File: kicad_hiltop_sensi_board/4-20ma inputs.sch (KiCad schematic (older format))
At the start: 44 parts, among them U12 MAX4194, U16 MAX4194, U19 MAX4194, U20 MAX4194

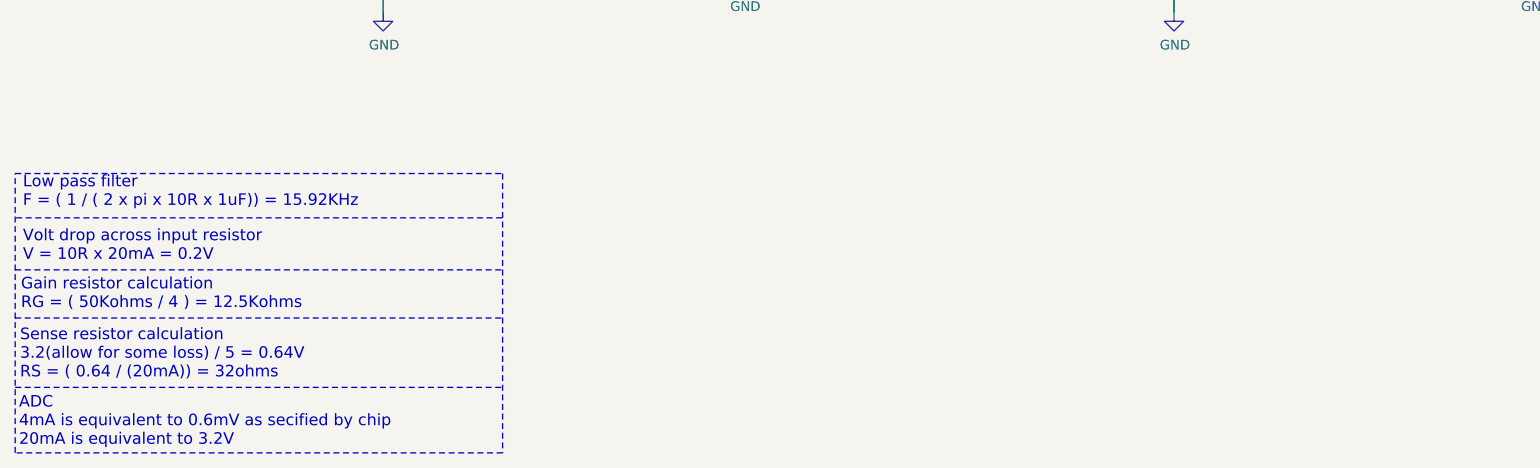
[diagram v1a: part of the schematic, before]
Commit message: Pressure sensor calcs added to 4-20mA circuit
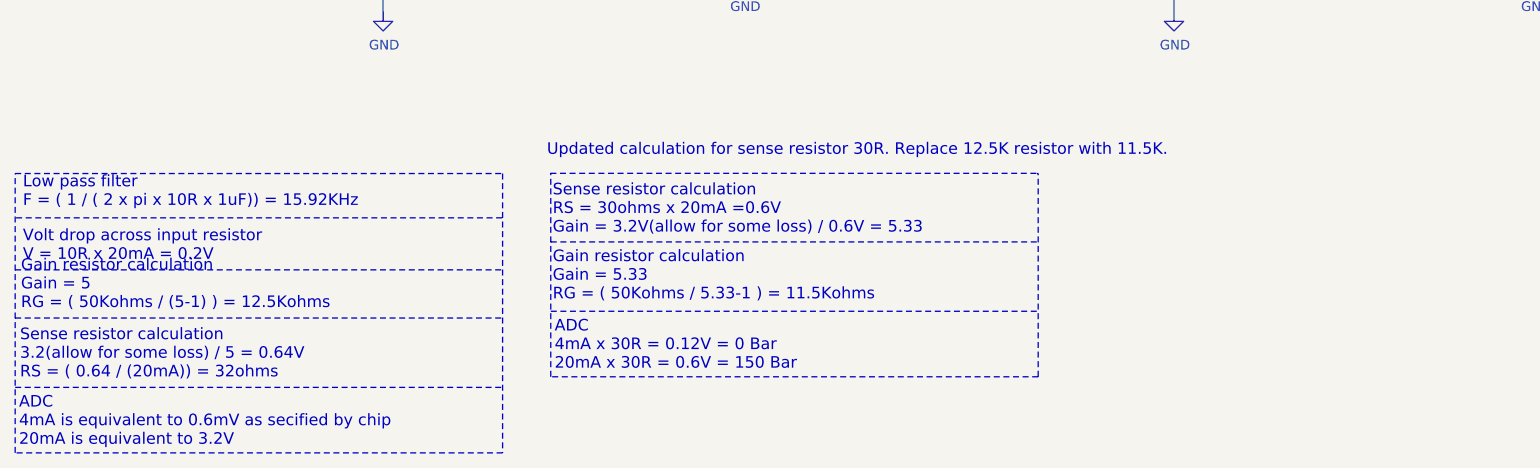
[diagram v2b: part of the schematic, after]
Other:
- note added: "ADC\n4mA x 30R = 0.12V = 0 Bar\n20mA x 30R = 0.6V = 150 Bar"
- note added: "Gain resistor calculation\nGain = 5.33\nRG = ( 50Kohms / 5.33-1 ) = 11.5Kohms"
- note added: "Gain resistor calculation\nGain = 5\nRG = ( 50Kohms / (5-1) ) = 12.5Kohms"
- note added: "Sense resistor calculation\nRS = 30ohms x 20mA =0.6V\nGain = 3.2V(allow for some loss) / 0.6V = 5.33\n\n"
- note added: "Updated calculation for sense resistor 30R. Replace 12.5K resistor with 11.5K."
- note removed: "Gain resistor calculation\nRG = ( 50Kohms / 4 ) = 12.5Kohms"
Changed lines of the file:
@@
 EESchema Schematic File Version 4
 LIBS:Sensi_Board-cache
-EELAYER 29 0
+EELAYER 30 0
 EELAYER END
 $Descr A4 11693 8268
@@
 Volt drop across input resistor\nV = 10R x 20mA = 0.2V
 Text Notes 870  6750 0    60   ~ 0
-Gain resistor calculation\nRG = ( 50Kohms / 4 ) = 12.5Kohms
+Gain resistor calculation\nGain = 5\nRG = ( 50Kohms / (5-1) ) = 12.5Kohms
 Text Notes 865  7110 0    60   ~ 0
 Sense resistor calculation\n3.2(allow for some loss) / 5 = 0.64V\nRS = ( 0.64 / (20mA)) = 32ohms\n
@@
 	7240 4250 8330 4250
 Connection ~ 7240 4250
+Text Notes 3630 6705 0    60   ~ 0
+Gain resistor calculation\nGain = 5.33\nRG = ( 50Kohms / 5.33-1 ) = 11.5Kohms
+Text Notes 3630 6455 0    60   ~ 0
+Sense resistor calculation\nRS = 30ohms x 20mA =0.6V\nGain = 3.2V(allow for some loss) / 0.6V = 5.33\n\n
+Text Notes 3640 7065 0    60   ~ 0
+ADC\n4mA x 30R = 0.12V = 0 Bar\n20mA x 30R = 0.6V = 150 Bar
+Wire Notes Line
+	6150 7095 3620 7095
+Wire Notes Line
+	3618 6039 6148 6039
+Wire Notes Line
+	3620 6395 6150 6395
+Wire Notes Line
+	3620 6755 6150 6755
+Wire Notes Line
+	3620 7095 3620 6040
+Wire Notes Line
+	6150 7095 6150 6040
+Wire Notes Line
+	6150 6040 6145 6040
+Text Notes 3600 5955 0    60   ~ 0
+Updated calculation for sense resistor 30R. Replace 12.5K resistor with 11.5K.
 $EndSCHEMATC
